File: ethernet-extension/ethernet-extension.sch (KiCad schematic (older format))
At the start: 43 parts, among them J1 Wuerth_7499010121A, J2 East, J3 West, U1 W5500, Y1 25MHz

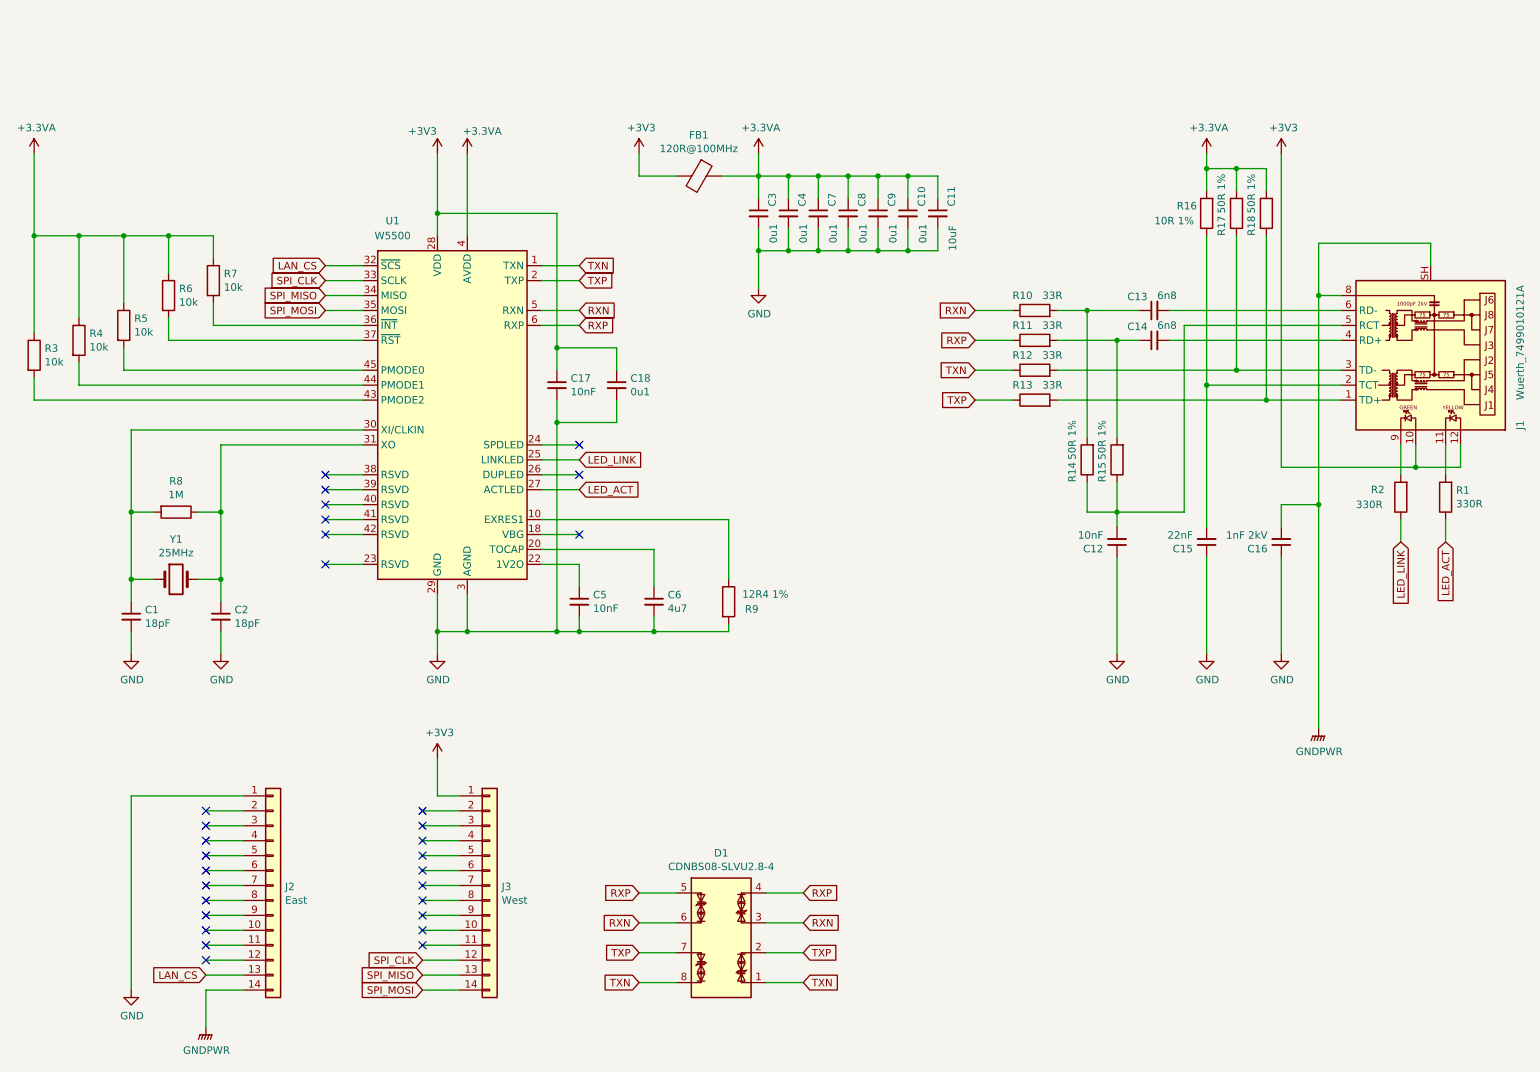
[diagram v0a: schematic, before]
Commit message: Work on Ethernet module
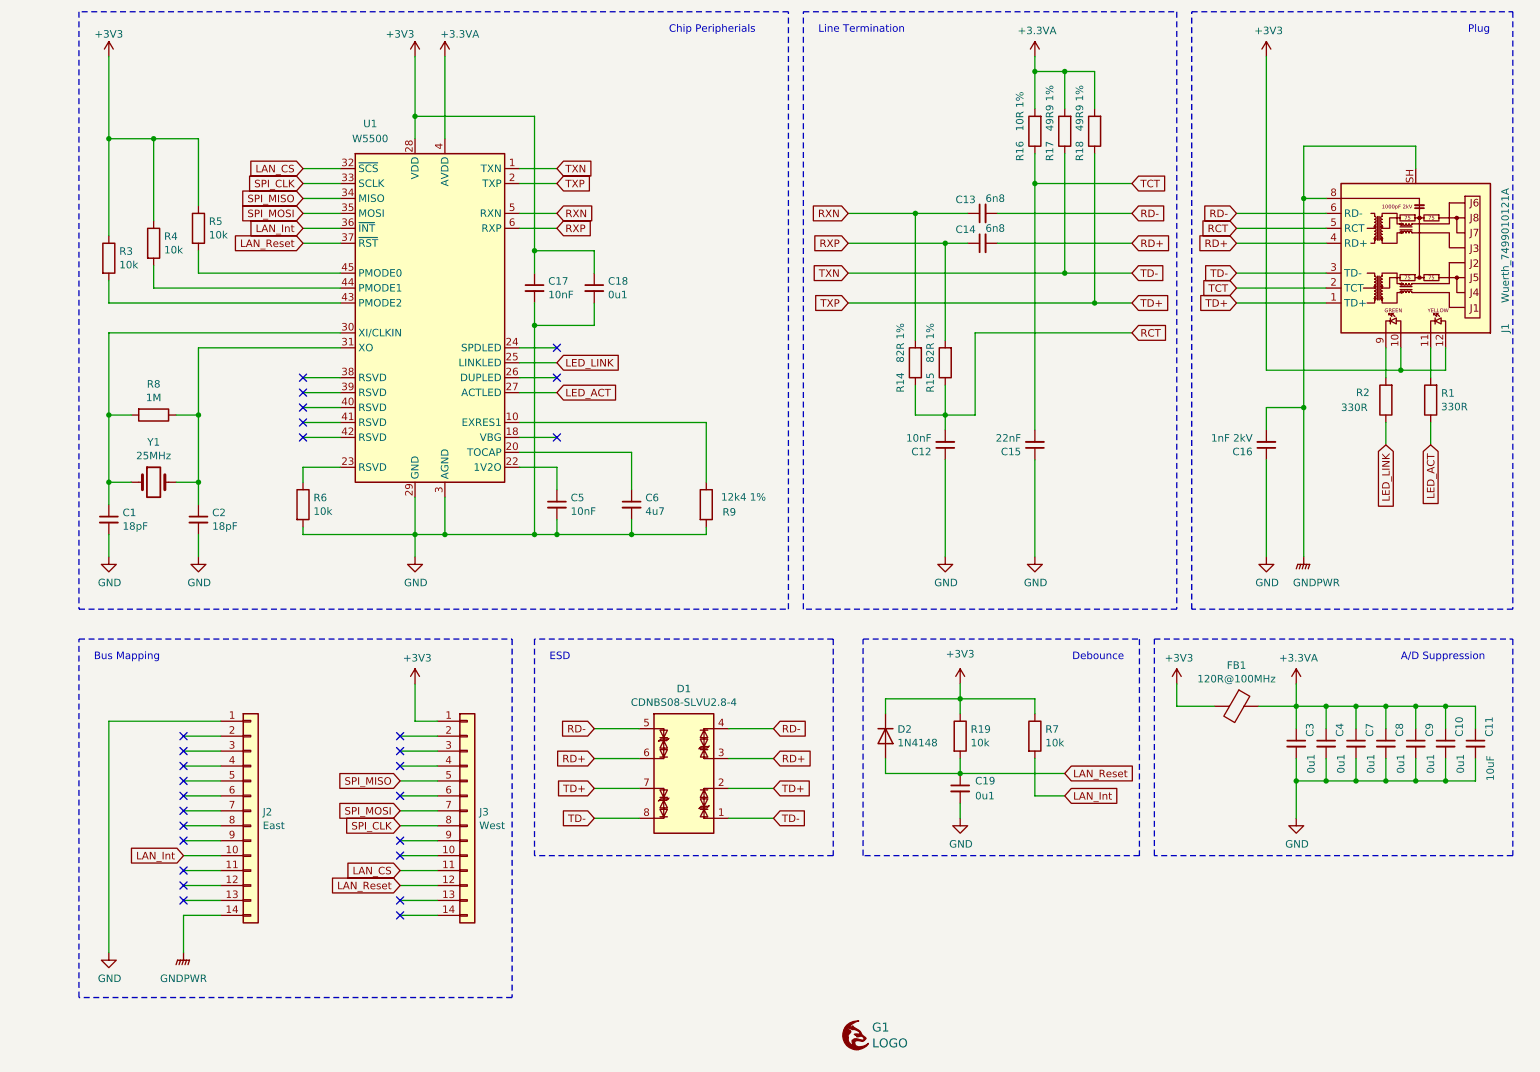
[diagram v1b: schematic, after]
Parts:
- removed R10, R11, R12, R13: 33R, Resistor_SMD:R_0603_1608Metric_Pad0.98x0.95mm_HandSolder, symbol Device:R
- added C19: 0u1, Capacitor_SMD:C_0603_1608Metric_Pad1.08x0.95mm_HandSolder, symbol Device:C_Small
- added D2: 1N4148, Diode_SMD:D_SOD-323_HandSoldering, symbol Diode:1N4148
- added G1: LOGO, footprints:grayc-logo-negative, symbol grayc-logo-negative:LOGO
- added R19: 10k, Resistor_SMD:R_0603_1608Metric_Pad0.98x0.95mm_HandSolder, symbol Device:R
- C16: Price (none) -> 1.21; Product (none) -> https://www.mouser.de/ProductDetail/KEMET/C1812C103KGRACTU
- FB1: Price (none) -> 0.08; Product (none) -> https://www.mouser.de/ProductDetail/Laird-Performance-Mater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
- J1: Price (none) -> 5.81; Product (none) -> https://www.mouser.de/ProductDetail/Wurth-Elektronik/749901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
- J2, J3: Price (none) -> 0; Product (none) -> N/A
- R14, R15: value 50R 1% -> 82R 1%
- R17, R18: value 50R 1% -> 49R9 1%
- R9: value 12R4 1% -> 12k4 1%
- U1: Price (none) -> 3.44; Product (none) -> https://www.mouser.de/ProductDetail/WIZnet/W5500
- Y1: Price (none) -> 0.98; Product (none) -> https://www.mouser.de/ProductDetail/ECS/ECS-250-18-23A-TR
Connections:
- net TXN is gone; now on net TD-: D1.1 (TVS1), D1.8 (TVS2), U1.1 (TXN)
- net TXP is gone; now on net TD+: D1.2 (TVS2), D1.7 (TVS1), U1.2 (TXP)
- net +3.3VA: no longer R3.1, R4.1, R5.1, R6.1, R7.1
- net +3V3: now also R3.1, R4.1, R5.1, R7.1, D2.1 (K), R19.1
- net GND: now also R6.2, C19.2
- net LAN_CS: now also J3.11 (Pin_11); no longer J2.13 (Pin_13)
- net RXN: now also C13.1, R14.2; no longer D1.3 (TVS1), D1.6 (TVS2)
- net RXP: now also C14.1, R15.2; no longer D1.4 (TVS2), D1.5 (TVS1)
- net SPI_CLK: now also J3.8 (Pin_8); no longer J3.12 (Pin_12)
- net SPI_MISO: now also J3.5 (Pin_5); no longer J3.13 (Pin_13)
- net SPI_MOSI: now also J3.7 (Pin_7); no longer J3.14 (Pin_14)
- net at U1.23 (RSVD): now also R6.1
- net LAN_Int: now reaches R7.2, U1.36 (~INT)
- net LAN_Int: now also J2.10 (Pin_10)
- net LAN_Reset: now reaches U1.37 (~RST)
- net LAN_Reset: now also J3.12 (Pin_12), C19.1, D2.2 (A), R19.2; no longer R6.2
- net RD+: now reaches C14.2, J1.4 (RD+)
- net RD+: now also D1.3 (TVS1), D1.6 (TVS2)
- net RD-: now reaches C13.2, J1.6 (RD-)
- net RD-: now also D1.4 (TVS2), D1.5 (TVS1)
- net TCT: now reaches C15.2, J1.2 (TCT), R16.1
- net TD-: now reaches J1.3 (TD-), R17.1
- net TD+: now reaches J1.1 (TD+), R18.1
- net RCT: now reaches C12.2, J1.5 (RCT), R14.1, R15.1
- no-connect marks 30 -> 27
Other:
- note added: "A/D Suppression"
- note added: "Bus Mapping"
- note added: "Chip Peripherials"
- note added: "Debounce"
- note added: "ESD"
- note added: "Line Termination"
- note added: "Plug"
- moved on the sheet: C1, C10, C11, C12, C13, C14, C15, C16, C17, C18, C2, C5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

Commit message: Added Panel Module to build
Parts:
- D1: Price (none) -> 1.68; Products (none) -> https://www.mouser.de/ProductDetail/Bourns/CDNBS08-SLVU28-4
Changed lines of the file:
@@
 F 2 "Package_SO:SOIC-8_3.9x4.9mm_P1.27mm" H 5350 5250 50  0001 C CNN
 F 3 "https://www.bourns.com/pdfs/CDNBS08-SLVU28-4.pdf" H 5400 5100 50  0001 C CNN
+F 4 "https://www.mouser.de/ProductDetail/Bourns/CDNBS08-SLVU28-4" H 5350 5800 50  0001 C CNN "Products"
+F 5 "1.68" H 5350 5800 50  0001 C CNN "Price"
 	1    5350 5800
 	1    0    0    -1

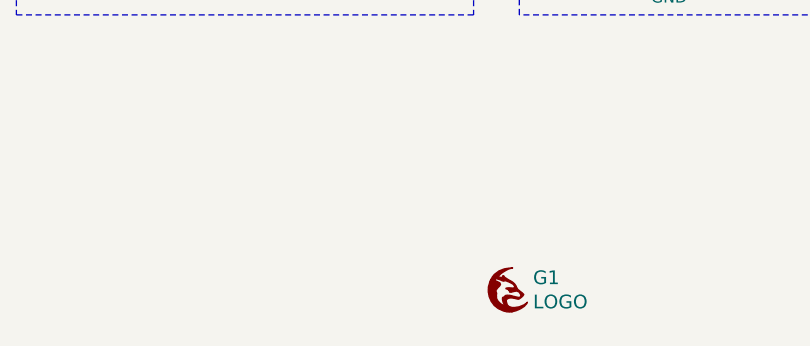
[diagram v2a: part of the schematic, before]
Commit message: Added OpenHardware Logo to PCBs
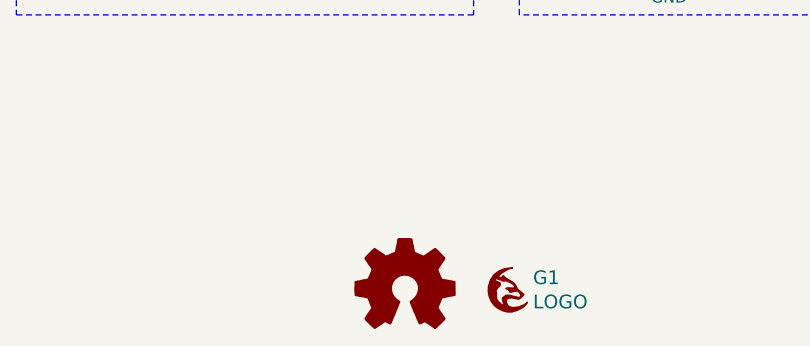
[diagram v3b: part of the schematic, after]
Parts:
- added G2: Logo_Open_Hardware_Small, Symbol:OSHW-Logo2_7.3x6mm_SilkScreen, symbol Graphic:Logo_Open_Hardware_Small
- C1, C2: Price (none) -> 0.09; Product (none) -> https://www.mouser.de/ProductDetail/Kyocera-AVX/06035A180JA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
- C10, C18, C19, C3, C4, C7, C8, C9: Price (none) -> 0.09; Product (none) -> https://www.mouser.de/ProductDetail/KEMET/C0603C104M4RACTU
- C11: Price (none) -> 0.10; Product (none) -> https://www.mouser.de/ProductDetail/Samsung-Electro-Mechani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
- C12, C17, C5: Price (none) -> 0.09; Product (none) -> https://www.mouser.de/ProductDetail/Kyocera-AVX/06031C103K4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
- C13, C14: Price (none) -> 0.09; Product (none) -> https://www.mouser.de/ProductDetail/KEMET/C0603C682K5RACTU
- C15, C6: Price (none) -> 0.09; Product (none) -> https://www.mouser.de/ProductDetail/Samsung-Electro-Mechani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
- D1: Product (none) -> https://www.mouser.de/ProductDetail/Bourns/CDNBS08-SLVU28-4; Products https://www.mouser.de/ProductDetail/Bourns/CDNBS08-SLVU28-4 -> (none)
- D2: Price (none) -> 0.12; Product (none) -> https://www.mouser.de/ProductDetail/Panjit/1N4148WS_R1_00001
- J2, J3: Price 0 -> 2.40; Product N/A -> https://www.mouser.de/ProductDetail/Preci-dip/801-87-014-53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
- R1, R2: Price (none) -> 0.09; Product (none) -> https://www.mouser.de/ProductDetail/Bourns/CR0603-FX-3300EL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
- R14, R15: Price (none) -> 0.09; Product (none) -> https://www.mouser.de/ProductDetail/Panasonic/ERJ-3EKF82R0V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
- R16: Price (none) -> 0.09; Product (none) -> https://www.mouser.de/ProductDetail/YAGEO/RC0603FR-1310RL?q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
- R17, R18: Price (none) -> 0.09; Product (none) -> https://www.mouser.de/ProductDetail/Panasonic/ERJ-3EKF49R9V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
- R19, R3, R4, R5, R6, R7: Product (none) -> https://www.mouser.de/ProductDetail/Bourns/CR0603AFX-1002EA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
- R8: Product (none) -> https://www.mouser.de/ProductDetail/Bourns/CMP0603-FX-1004E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
- R9: Price (none) -> 0.09; Product (none) -> https://www.mouser.de/ProductDetail/Bourns/CR0603-FX-1242EL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
